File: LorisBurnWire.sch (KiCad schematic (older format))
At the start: 23 parts, among them U2 TLC555ID, U3 TLC555ID

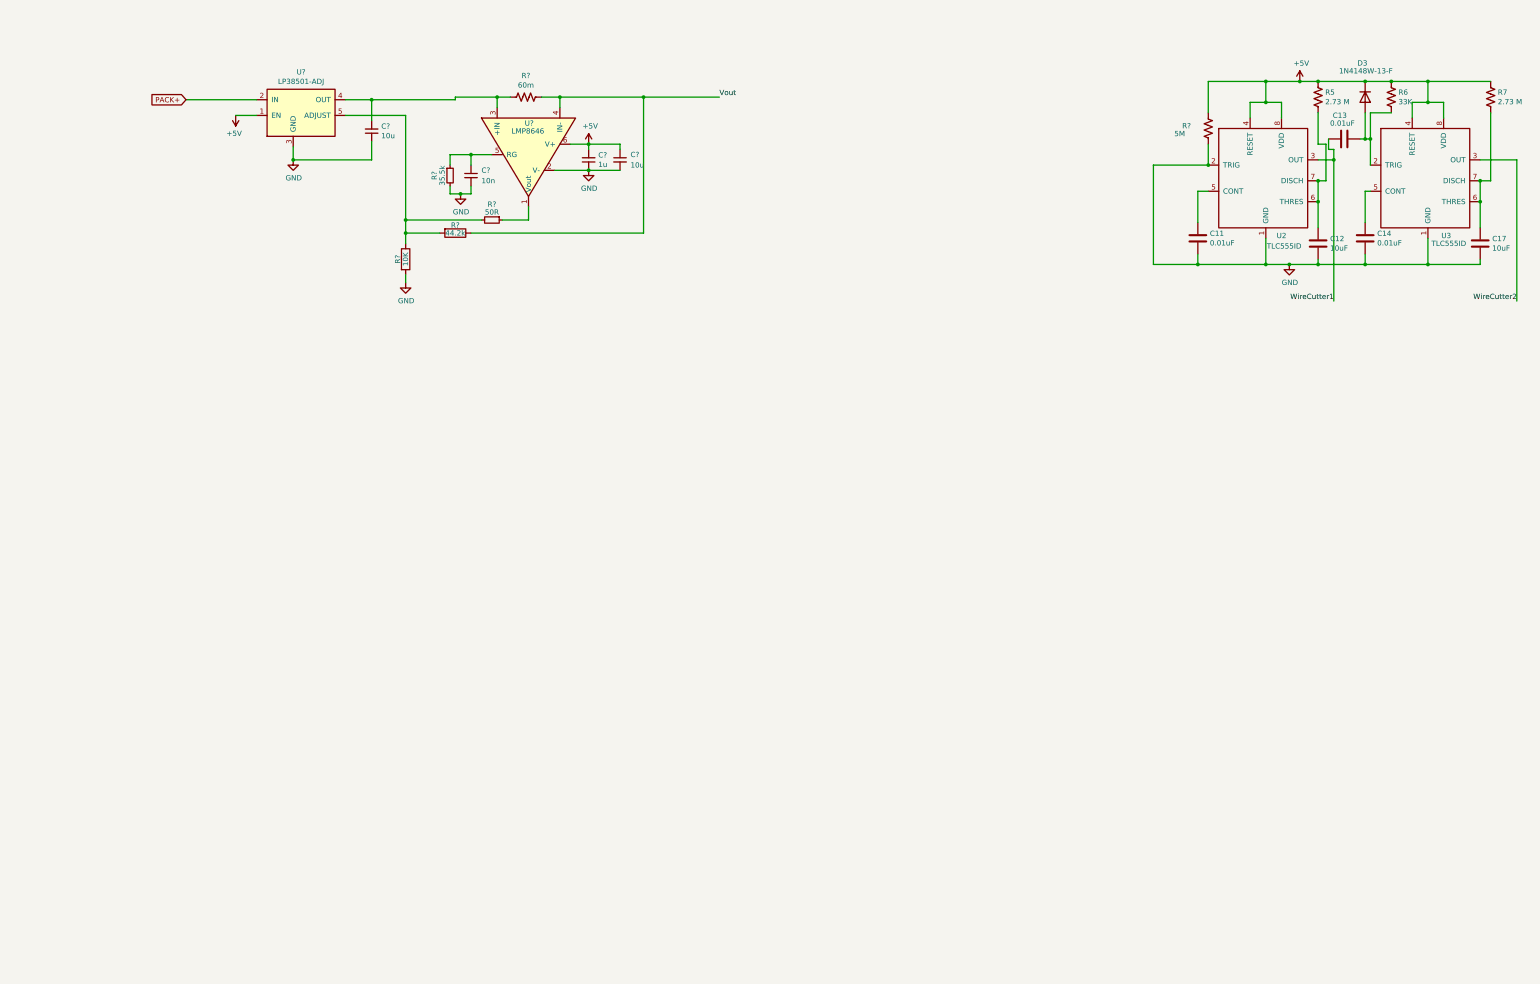
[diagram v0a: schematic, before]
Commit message: added powerfet
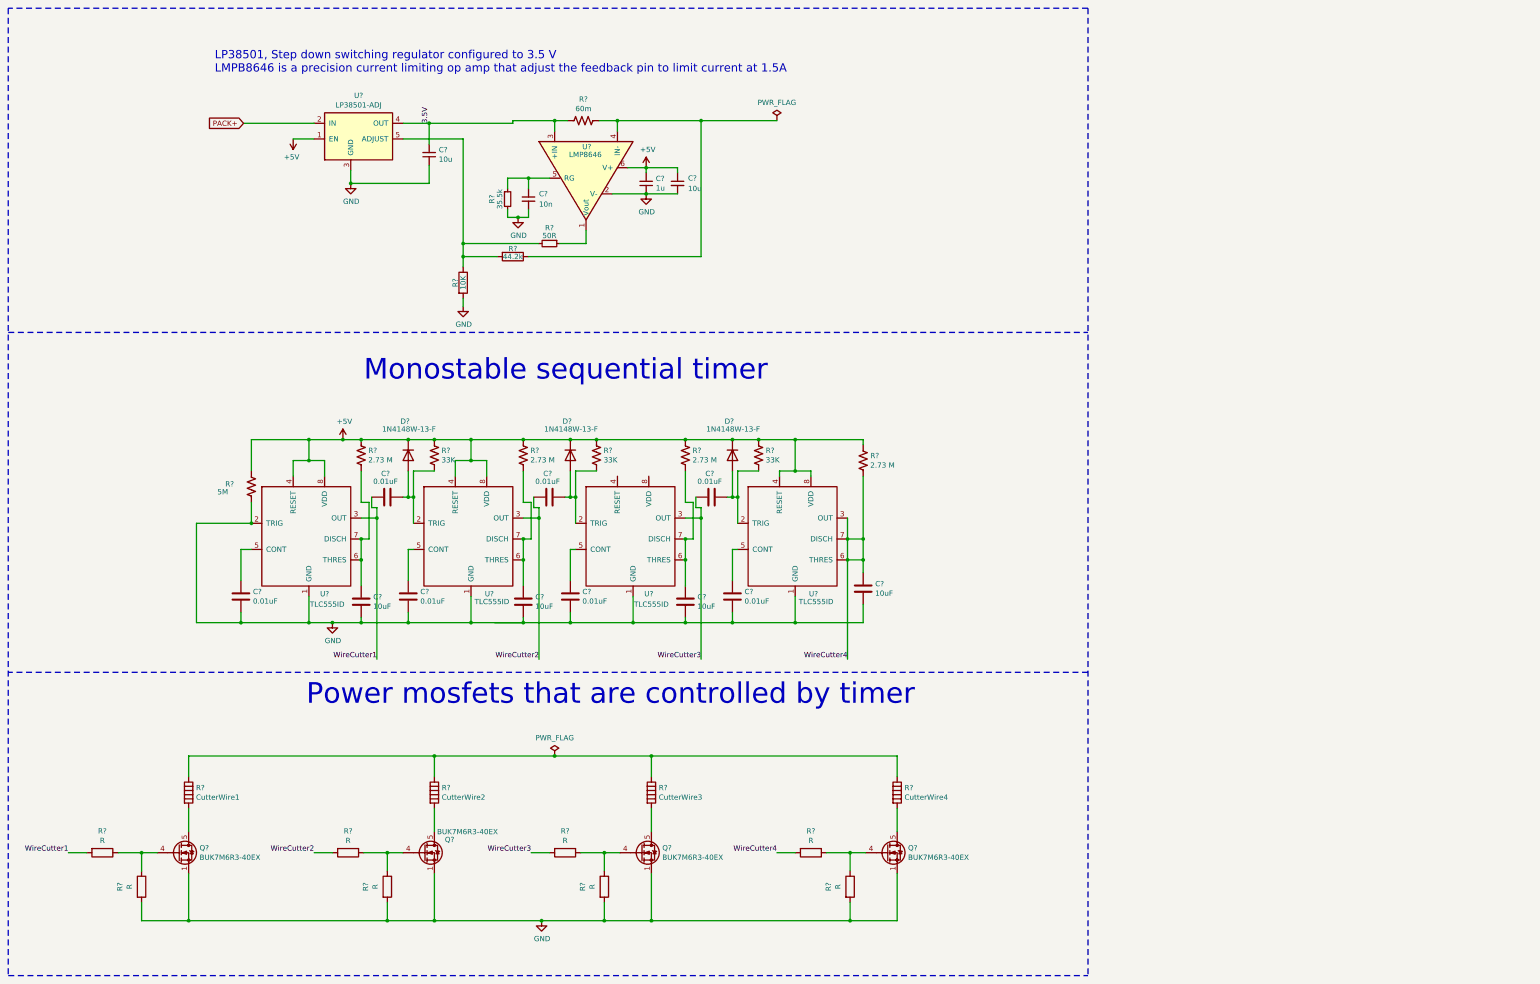
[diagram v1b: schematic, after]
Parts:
- removed C11, C13, C14: 0.01uF, Capacitor_SMD:C_1206_3216Metric_Pad1.42x1.75mm_HandSolder, symbol Device:C
- removed C12, C17: 10uF, Capacitor_SMD:C_1206_3216Metric_Pad1.42x1.75mm_HandSolder, symbol Device:C
- removed D3: 1N4148W-13-F, Diodes_SMD:D_SOD-123, symbol Device:D
- removed R5, R7: 2.73 M, Resistor_SMD:R_1206_3216Metric_Pad1.42x1.75mm_HandSolder, symbol Device:R_US
- removed R6: 33K, Resistor_SMD:R_1206_3216Metric_Pad1.42x1.75mm_HandSolder, symbol Device:R_US
- removed R?: 5M, Resistor_SMD:R_1206_3216Metric_Pad1.42x1.75mm_HandSolder, symbol Device:R_US
- removed U2, U3: TLC555ID, Housings_SOIC:SOIC-8_3.9x4.9mm_Pitch1.27mm, symbol LorisBurnWire-rescue:TLC555-Loris
- added C? (x7): 0.01uF, Capacitor_SMD:C_1206_3216Metric_Pad1.42x1.75mm_HandSolder, symbol Device:C
- added C? (x4): 10uF, Capacitor_SMD:C_1206_3216Metric_Pad1.42x1.75mm_HandSolder, symbol Device:C
- added D? (x3): 1N4148W-13-F, Diodes_SMD:D_SOD-123, symbol Device:D
- added Q? (x4): BUK7M6R3-40EX, Package_TO_SOT_SMD:LFPAK33, symbol Transistor_FET:BUK7M6R3-40EX
- added R? (x4): 2.73 M, Resistor_SMD:R_1206_3216Metric_Pad1.42x1.75mm_HandSolder, symbol Device:R_US
- added R? (x3): 33K, Resistor_SMD:R_1206_3216Metric_Pad1.42x1.75mm_HandSolder, symbol Device:R_US
- added R?: 5M, Resistor_SMD:R_1206_3216Metric_Pad1.42x1.75mm_HandSolder, symbol Device:R_US
- added R? (x8): R, symbol Device:R
- added R?: CutterWire1, symbol Device:Heater
- added R?: CutterWire2, symbol Device:Heater
- added R?: CutterWire3, symbol Device:Heater
- added R?: CutterWire4, symbol Device:Heater
- added U? (x4): TLC555ID, Housings_SOIC:SOIC-8_3.9x4.9mm_Pitch1.27mm, symbol LorisBurnWire-rescue:TLC555-Loris
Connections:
- net +5V: now also D?.1 (K), D?.1 (K), D?.1 (K), R?.1, R?.1, R?.1, R?.1, R?.1, R?.1, R?.1, R?.1, U?.4 (RESET), U?.4 (RESET), U?.4 (RESET), U?.8 (VDD), U?.8 (VDD), U?.8 (VDD)
- net GND: now also C?.2, C?.2, C?.2, C?.2, C?.2, C?.2, C?.2, C?.2, Q?.1 (S), Q?.1 (S), Q?.1 (S), Q?.1 (S), Q?.2 (S), Q?.2 (S), Q?.2 (S), Q?.2 (S), Q?.3 (S), Q?.3 (S), Q?.3 (S), Q?.3 (S), R?.2, R?.2, R?.2, R?.2, R?.2, U?.1 (GND), U?.1 (GND), U?.1 (GND), U?.1 (GND), U?.2 (TRIG)
- net WireCutter1: now also C?.1, R?.2, U?.3 (OUT)
- net WireCutter2: now also C?.1, R?.2, U?.3 (OUT)
- net 3.5V: now reaches C?.2, R?.2, U?.3 (+IN), U?.4 (OUT)
- net Vout: no longer names the net of R?.1, R?.1, U?.4 (IN-)
- new net: C?.1, U?.5 (CONT) (x4)
- new net: C?.1, R?.2, U?.6 (THRES), U?.7 (DISCH) (x3)
- new net: C?.2, D?.2 (A), R?.2, U?.2 (TRIG) (x3)
- new net: Q?.4 (G), R?.1, R?.1 (x4)
- new net: Q?.5 (D), R?.2 (x4)
- new net: R?.1, R?.1, R?.1, R?.1
- new net WireCutter3: C?.1, R?.2, U?.3 (OUT)
- new net WireCutter4: C?.1, R?.2, R?.2, U?.3 (OUT), U?.6 (THRES), U?.7 (DISCH)
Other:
- note added: "LP38501, Step down switching regulator configured to 3.5 V\nLMPB8646 is a precision current limiting op amp that adjust the feedback pin to limit current at 1.5A"
- note added: "Monostable sequential timer"
- note added: "Power mosfets that are controlled by timer"
- moved on the sheet: C?, R?, U?

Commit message: fixed mistake
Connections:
- net WireCutter4: no longer C?.1, R?.2, U?.6 (THRES), U?.7 (DISCH)
- new net: C?.1, R?.2, U?.6 (THRES), U?.7 (DISCH)
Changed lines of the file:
@@
 	8800 6575 8800 6400
 Connection ~ 8150 6575
-Wire Wire Line
-	8650 5575 8650 5775
-Connection ~ 8650 5775
-Wire Wire Line
-	8650 5775 8650 5975
-Connection ~ 8650 5975
-Wire Wire Line
-	8650 5975 8650 6925
-Text Label 8650 6925 2    50   ~ 0
+Text Label 8900 6900 2    50   ~ 0
 WireCutter4
 $Comp
@@
 	1900 9425 1900 9250
 Connection ~ 2350 9425
+Wire Wire Line
+	8650 5575 8900 5575
+Wire Wire Line
+	8900 5575 8900 6900
 $EndSCHEMATC

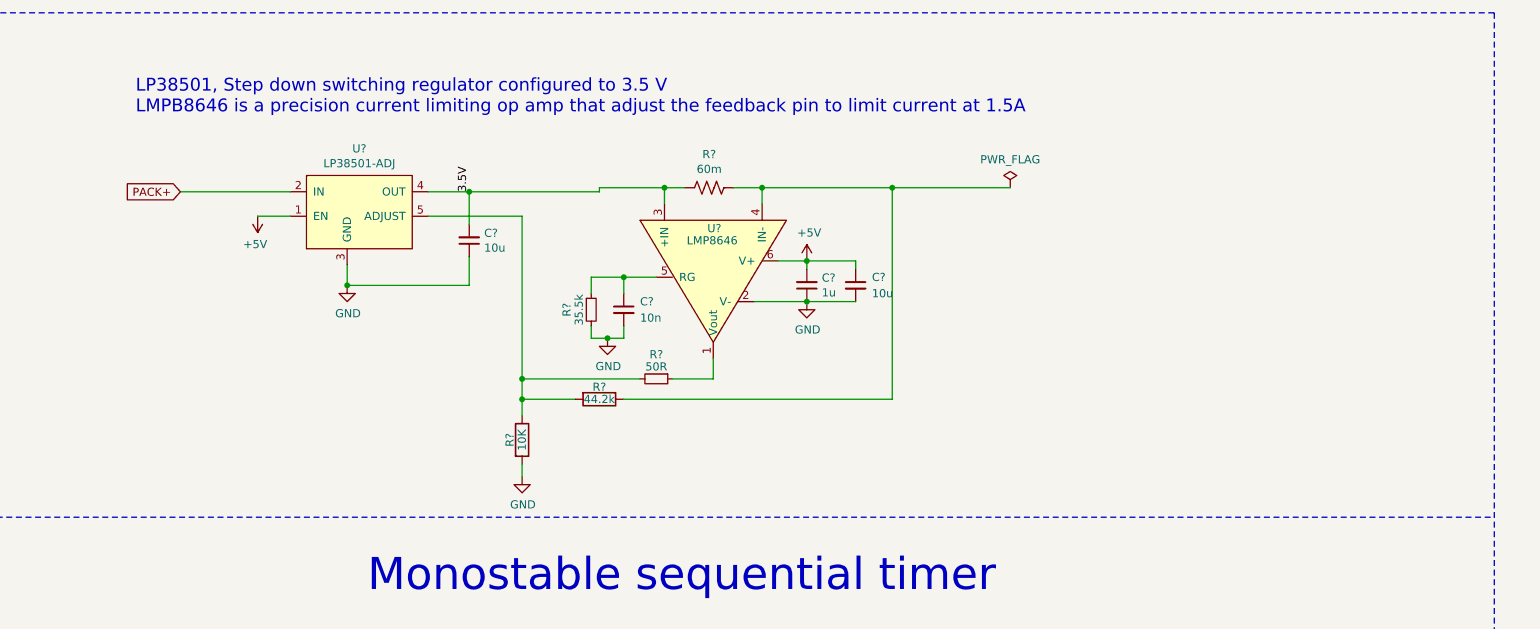
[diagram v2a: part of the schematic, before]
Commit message: added jumpers to turn regulator off and on
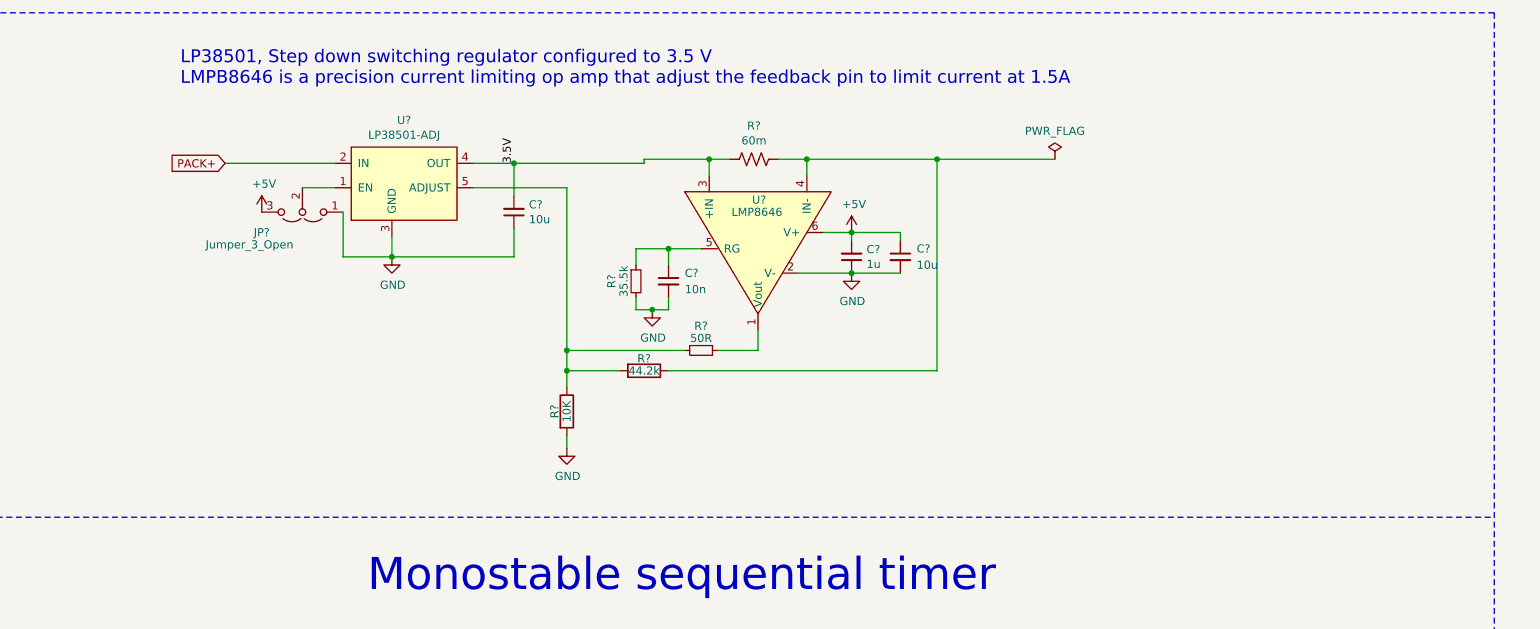
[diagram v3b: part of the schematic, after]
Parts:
- added JP?: Jumper_3_Open, symbol Jumper:Jumper_3_Open
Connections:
- net +5V: now also JP?.3 (B); no longer U?.1 (EN)
- net GND: now also JP?.1 (A)
- new net: JP?.2 (C), U?.1 (EN)
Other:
- moved on the sheet: C?, R?, U?

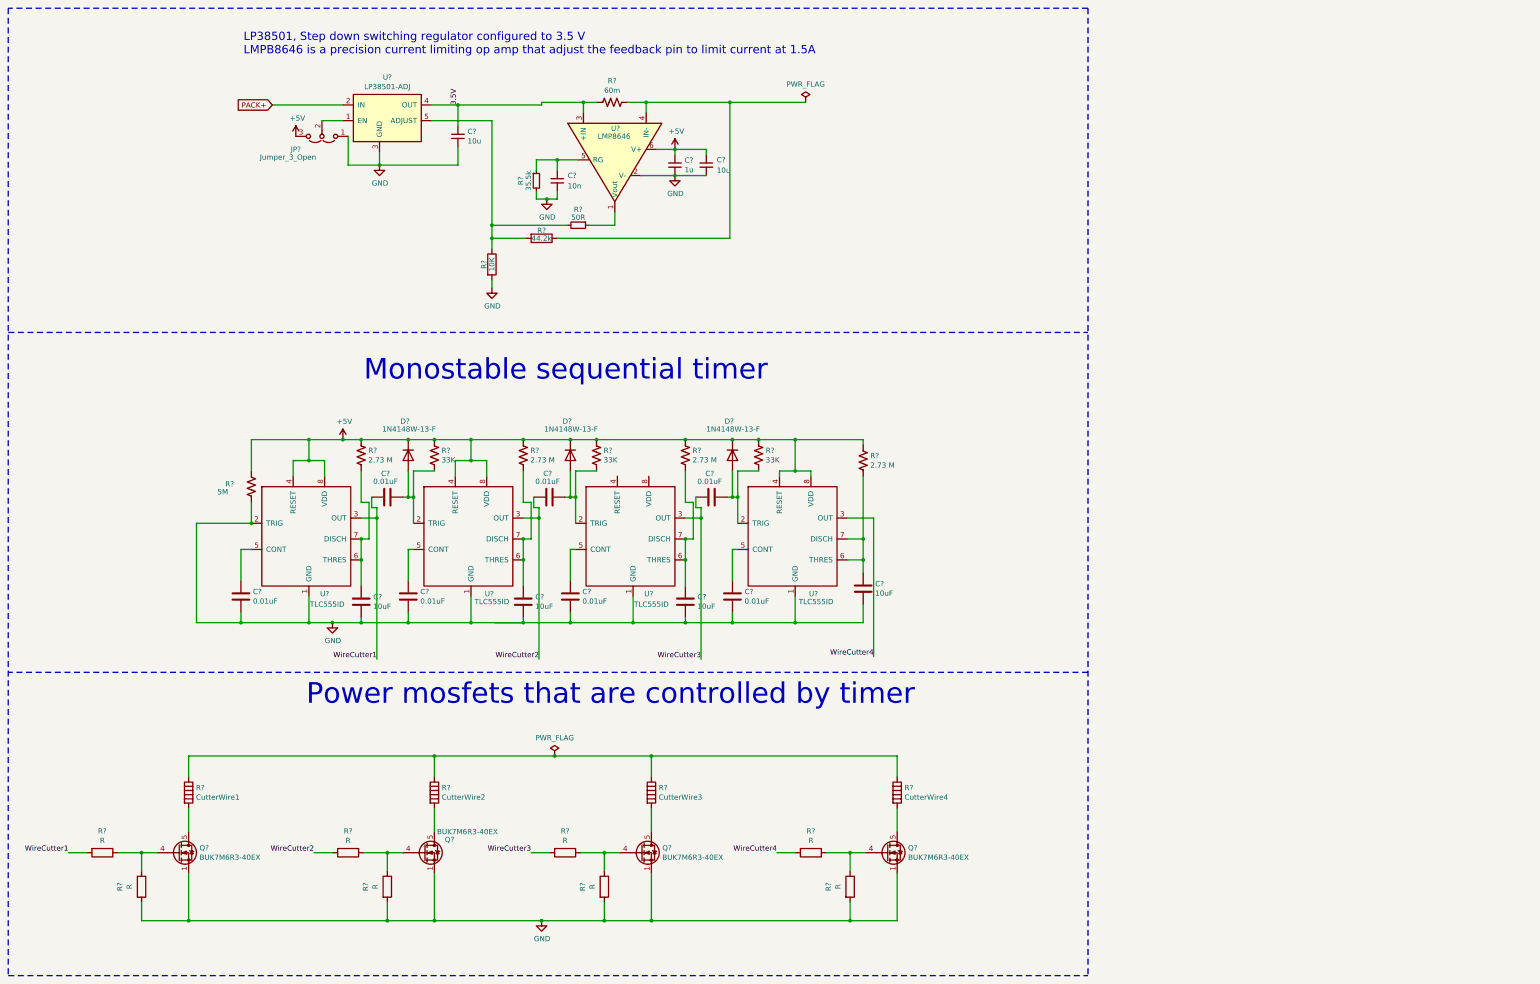
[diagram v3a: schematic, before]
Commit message: added resistor to fets and added screw terminals
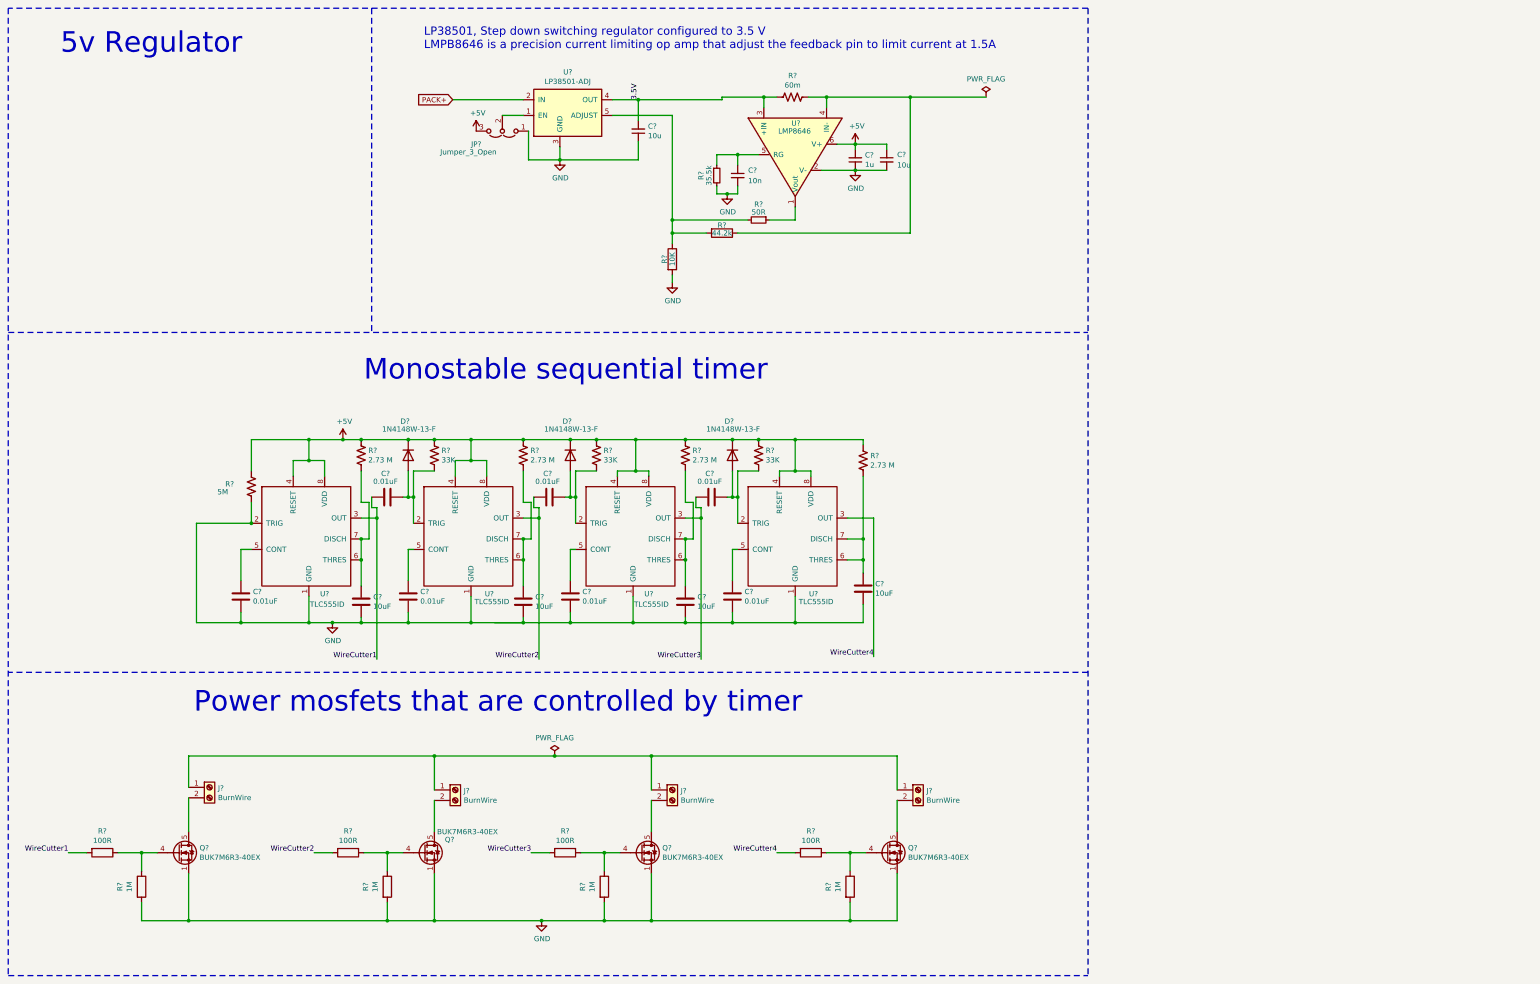
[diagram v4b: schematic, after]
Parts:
- removed R?: CutterWire1, symbol Device:Heater
- removed R?: CutterWire2, symbol Device:Heater
- removed R?: CutterWire3, symbol Device:Heater
- removed R?: CutterWire4, symbol Device:Heater
- added J? (x4): BurnWire, symbol Connector:Screw_Terminal_01x02
- R? (x4): value R -> 100R
- R? (x4): value R -> 1M
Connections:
- net +5V: now also U?.4 (RESET), U?.8 (VDD)
- net at Q?.5 (D): now also J?.2 (Pin_2) (x4)
- new net: J?.1 (Pin_1), J?.1 (Pin_1), J?.1 (Pin_1), J?.1 (Pin_1)
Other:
- note added: "5v Regulator"
- moved on the sheet: C?, JP?, R?, U?

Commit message: added footprints to all the resistors and capacitors
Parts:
- C12, C13, C15, C8: renamed from C?; footprint (none) -> Capacitor_SMD:C_1206_3216Metric_Pad1.42x1.75mm_HandSolder
- R1, R11, R12, R14, R15, R16, R18, R19, R2, R20, R4, R6, R9: renamed from R?; footprint (none) -> Resistor_SMD:R_1206_3216Metric_Pad1.42x1.75mm_HandSolder
- U3: renamed from U?; symbol BurnWireLib:LP38501-ADJ -> LorisBurnWire-rescue:LP38501-ADJ-BurnWireLib
- U5: renamed from U?; symbol BurnWireLib:LMP8646 -> LorisBurnWire-rescue:LMP8646-BurnWireLib
- gave numbers to parts that had none: 35

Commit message: Added footprint to burn wires
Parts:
- J1, J2, J3, J4: footprint (none) -> TerminalBlock_Phoenix:TerminalBlock_Phoenix_MKDS-3-2-5.08_1x02_P5.08mm_Horizontal
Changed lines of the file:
@@
 F 0 "J4" H 9405 8167 50  0000 L CNN
 F 1 "BurnWire" H 9405 8076 50  0000 L CNN
-F 2 "" H 9325 8175 50  0001 C CNN
+F 2 "TerminalBlock_Phoenix:TerminalBlock_Phoenix_MKDS-3-2-5.08_1x02_P5.08mm_Horizontal" H 9325 8175 50  0001 C CNN
 F 3 "~" H 9325 8175 50  0001 C CNN
 	1    9325 8175
@@
 F 0 "J3" H 7055 8167 50  0000 L CNN
 F 1 "BurnWire" H 7055 8076 50  0000 L CNN
-F 2 "" H 6975 8175 50  0001 C CNN
+F 2 "TerminalBlock_Phoenix:TerminalBlock_Phoenix_MKDS-3-2-5.08_1x02_P5.08mm_Horizontal" H 6975 8175 50  0001 C CNN
 F 3 "~" H 6975 8175 50  0001 C CNN
 	1    6975 8175
@@
 F 0 "J2" H 4980 8167 50  0000 L CNN
 F 1 "BurnWire" H 4980 8076 50  0000 L CNN
-F 2 "" H 4900 8175 50  0001 C CNN
+F 2 "TerminalBlock_Phoenix:TerminalBlock_Phoenix_MKDS-3-2-5.08_1x02_P5.08mm_Horizontal" H 4900 8175 50  0001 C CNN
 F 3 "~" H 4900 8175 50  0001 C CNN
 	1    4900 8175
@@
 F 0 "J1" H 2630 8142 50  0000 L CNN
 F 1 "BurnWire" H 2630 8051 50  0000 L CNN
-F 2 "" H 2550 8150 50  0001 C CNN
+F 2 "TerminalBlock_Phoenix:TerminalBlock_Phoenix_MKDS-3-2-5.08_1x02_P5.08mm_Horizontal" H 2550 8150 50  0001 C CNN
 F 3 "~" H 2550 8150 50  0001 C CNN
 	1    2550 8150
